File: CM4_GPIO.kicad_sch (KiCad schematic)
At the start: 13 parts, among them J10 Conn_01x03, J4 THD-20-R, J9 Conn_01x03, U12 SI-51005-F, U2 74LVC1G07SE-7

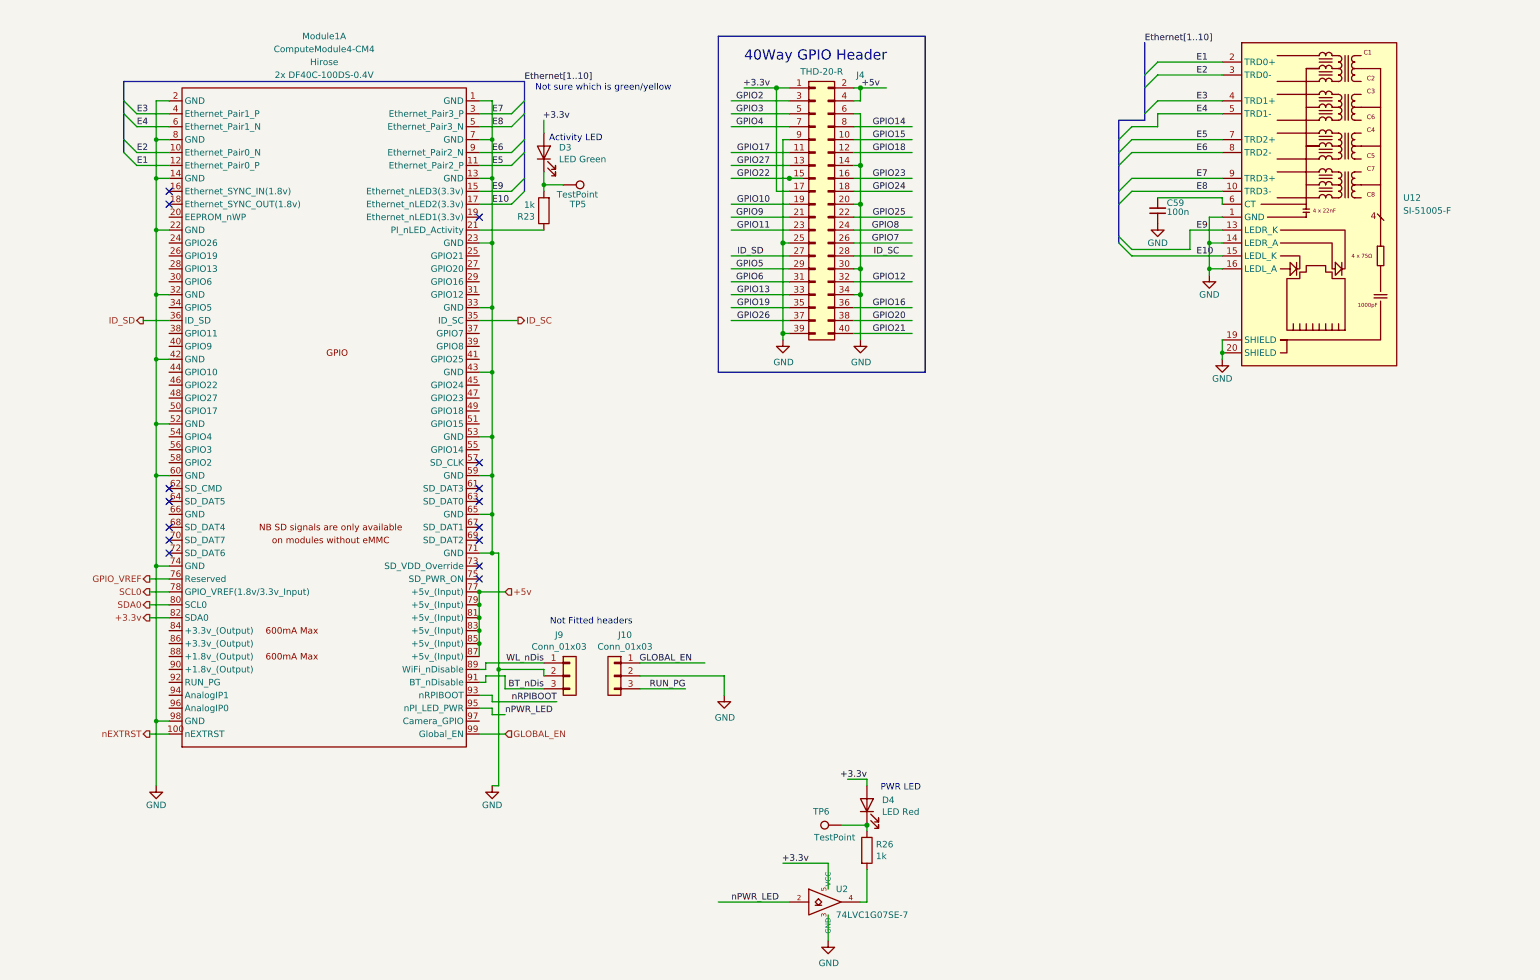
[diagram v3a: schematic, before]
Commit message: Added 3d-models, esd protection, cleaned up and made small start with pcb
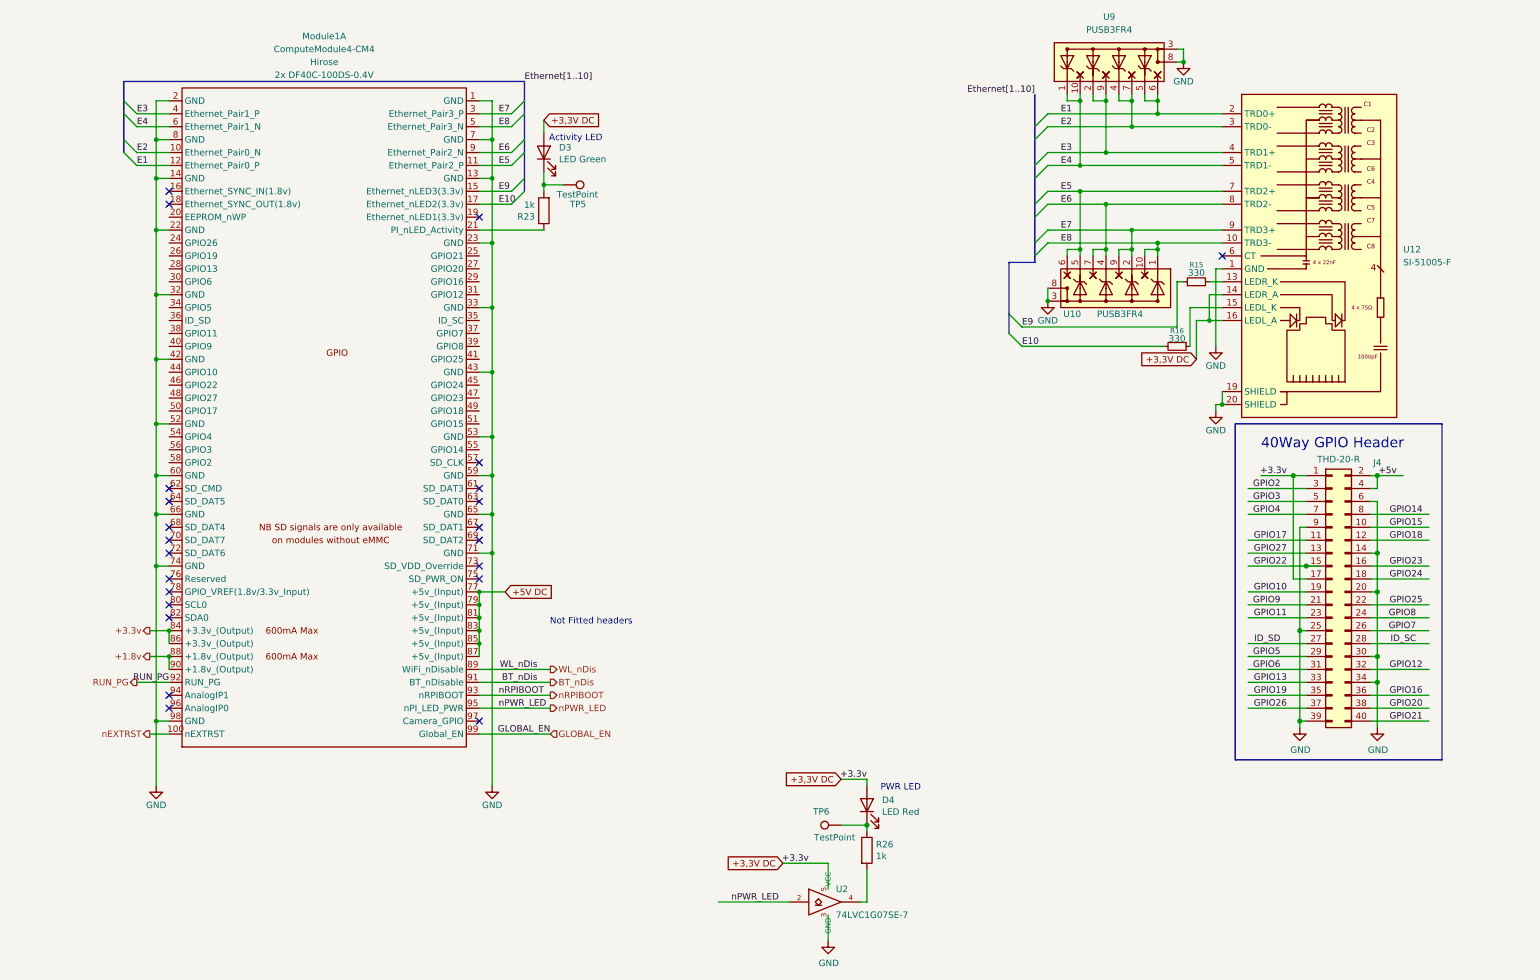
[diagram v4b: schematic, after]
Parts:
- removed C59: 100n, symbol Device:C_Small
- removed J10, J9: Conn_01x03, Connector_PinHeader_2.54mm:PinHeader_1x03_P2.54mm_Vertical, symbol Connector_Generic:Conn_01x03
- added R15, R16: 330, Resistor_SMD:R_0603_1608Metric, symbol Device:R_Small
- added U10, U9: PUSB3FR4, lib:SOT1176-1, symbol PUSB3FR4:PUSB3FR4
- Module1: footprint CM4IO:Raspberry-Pi-4-Compute-Module -> ComputeModule4:Raspberry-Pi-4-Compute-Module
- R23, R26: footprint Resistor_SMD:R_0402_1005Metric -> Resistor_SMD:R_0603_1608Metric
- U12: footprint Ethernet_con:TE_RJ45-8L-B -> SI-51005-F:BEL_SI-51005-F
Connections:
- net +5v: no longer Module1.77 (+5v_(Input)), Module1.79 (+5v_(Input)), Module1.81 (+5v_(Input)), Module1.83 (+5v_(Input)), Module1.85 (+5v_(Input)), Module1.87 (+5v_(Input))
- net E1: now also U9.5 (In_1-), U9.6 (Out_1+)
- net E2: now also U9.4 (In_1+), U9.7 (Out_1+)
- net E3: now also U9.2 (In_1-), U9.9 (Out_1+)
- net E4: now also U9.1 (In_1+), U9.10 (Out_1+)
- net GND: now also Module1.66 (GND), U10.3 (GND), U10.8 (GND), U9.3 (GND), U9.8 (GND); no longer Module1.11 (Ethernet_Pair2_P), Module1.15 (Ethernet_nLED3(3.3v)), Module1.17 (Ethernet_nLED2(3.3v)), Module1.3 (Ethernet_Pair3_P), Module1.5 (Ethernet_Pair3_N), Module1.9 (Ethernet_Pair2_N), U12.10 (TRD3-), U12.13 (LEDR_K), U12.14 (LEDR_A), U12.15 (LEDL_K), U12.16 (LEDL_A), U12.7 (TRD2+), U12.8 (TRD2-), U12.9 (TRD3+)
- net ID_SC: no longer Module1.35 (ID_SC)
- net ID_SD: no longer Module1.36 (ID_SD)
- net RUN_PG: now also Module1.92 (RUN_PG)
- net +3,3V DC: now reaches D3.2 (A)
- net +3,3V DC: now also D4.2 (A), J4.1 (Pin_1), J4.17 (Pin_17), Module1.84 (+3.3v_(Output)), Module1.86 (+3.3v_(Output)), U12.14 (LEDR_A), U12.16 (LEDL_A), U2.5 (VCC)
- net +1.8v: now reaches Module1.88 (+1.8v_(Output))
- net +1.8v: now also Module1.90 (+1.8v_(Output))
- removed net +3.3v: D4.2 (A), J4.1 (Pin_1), J4.17 (Pin_17), Module1.82 (SDA0), U2.5 (VCC)
- net GPIO_VREF: no longer names the net of Module1.76 (Reserved)
- net SCL0: no longer names the net of Module1.78 (GPIO_VREF(1.8v/3.3v_Input))
- net SDA0: no longer names the net of Module1.80 (SCL0)
- new net: R15.2, U12.13 (LEDR_K)
- new net: R16.1, U12.15 (LEDL_K)
- new net +5V DC: Module1.77 (+5v_(Input)), Module1.79 (+5v_(Input)), Module1.81 (+5v_(Input)), Module1.83 (+5v_(Input)), Module1.85 (+5v_(Input)), Module1.87 (+5v_(Input))
- new net E10: Module1.17 (Ethernet_nLED2(3.3v)), R16.2
- new net E5: Module1.11 (Ethernet_Pair2_P), U10.5 (In_1-), U10.6 (Out_1+), U12.7 (TRD2+)
- new net E6: Module1.9 (Ethernet_Pair2_N), U10.4 (In_1+), U10.7 (Out_1+), U12.8 (TRD2-)
- new net E7: Module1.3 (Ethernet_Pair3_P), U10.2 (In_1-), U10.9 (Out_1+), U12.9 (TRD3+)
- new net E8: Module1.5 (Ethernet_Pair3_N), U10.1 (In_1+), U10.10 (Out_1+), U12.10 (TRD3-)
- new net E9: Module1.15 (Ethernet_nLED3(3.3v)), R15.1
- no-connect marks 15 -> 23
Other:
- note removed: "Not sure which is green/yellow"
- moved on the sheet: J4, U12

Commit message: Adjusted the PCB design, changed footprints to 0402 (temp)
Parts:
- R15, R16, R23, R26: footprint Resistor_SMD:R_0603_1608Metric -> Resistor_SMD:R_0402_1005Metric_Pad0.72x0.64mm_HandSolder
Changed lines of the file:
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@@
 			)
 		)
-		(property "Footprint" "Resistor_SMD:R_0603_1608Metric"
+		(property "Footprint" "Resistor_SMD:R_0402_1005Metric_Pad0.72x0.64mm_HandSolder"
 			(at 103.378 48.26 90)
 			(effects
@@
 			)
 		)
-		(property "Footprint" "Resistor_SMD:R_0603_1608Metric"
+		(property "Footprint" "Resistor_SMD:R_0402_1005Metric_Pad0.72x0.64mm_HandSolder"
 			(at 163.322 173.99 90)
 			(effects
@@
 			)
 		)
-		(property "Footprint" "Resistor_SMD:R_0603_1608Metric"
+		(property "Footprint" "Resistor_SMD:R_0402_1005Metric_Pad0.72x0.64mm_HandSolder"
 			(at 226.06 74.93 0)
 			(effects
@@
 			)
 		)
-		(property "Footprint" "Resistor_SMD:R_0603_1608Metric"
+		(property "Footprint" "Resistor_SMD:R_0402_1005Metric_Pad0.72x0.64mm_HandSolder"
 			(at 229.87 62.23 0)
 			(effects

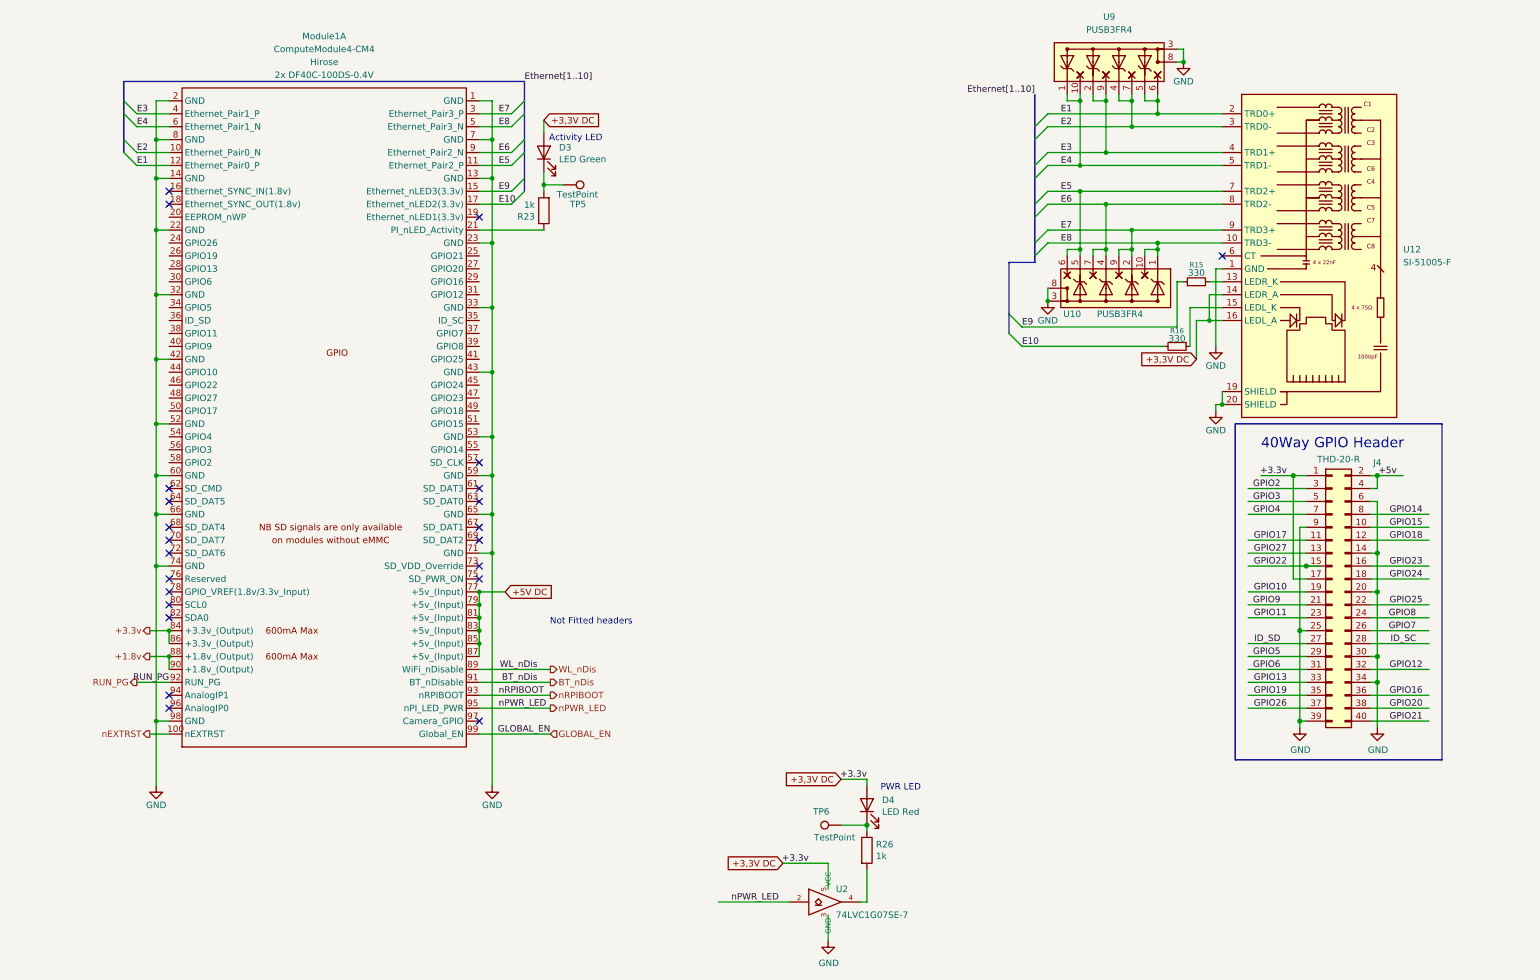
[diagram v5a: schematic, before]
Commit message: heb de GPIO aangepast.
Laten we morgen de stand van zaken bespreken. En overleggen wat we kunnen doen
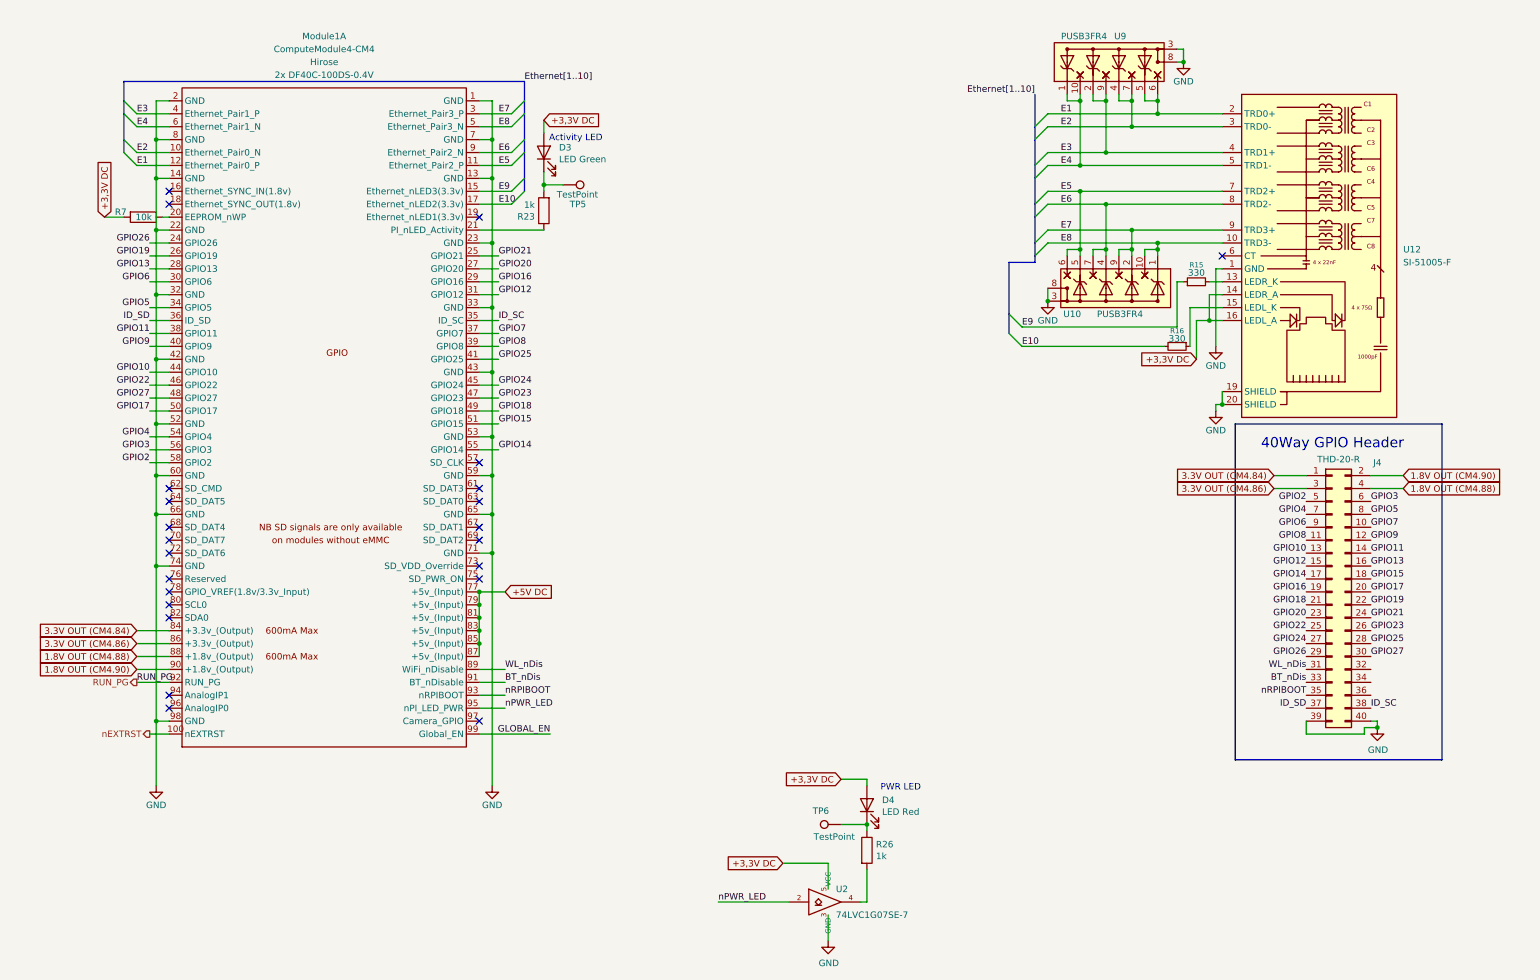
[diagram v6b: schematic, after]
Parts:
- added R7: 10k, Resistor_SMD:R_0402_1005Metric_Pad0.72x0.64mm_HandSolder, symbol Device:R
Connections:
- net +3,3V DC: now also R7.2; no longer J4.1 (Pin_1), J4.17 (Pin_17), Module1.84 (+3.3v_(Output)), Module1.86 (+3.3v_(Output))
- net BT_nDis: now also J4.33 (Pin_33)
- net GND: now also J4.40 (Pin_40); no longer J4.14 (Pin_14), J4.20 (Pin_20), J4.25 (Pin_25), J4.30 (Pin_30), J4.34 (Pin_34), J4.6 (Pin_6), J4.9 (Pin_9)
- net GPIO10: now also J4.13 (Pin_13), Module1.44 (GPIO10); no longer J4.19 (Pin_19)
- net GPIO11: now also J4.14 (Pin_14), Module1.38 (GPIO11); no longer J4.23 (Pin_23)
- net GPIO12: now also J4.15 (Pin_15), Module1.31 (GPIO12); no longer J4.32 (Pin_32)
- net GPIO13: now also J4.16 (Pin_16), Module1.28 (GPIO13); no longer J4.33 (Pin_33)
- net GPIO14: now also J4.17 (Pin_17), Module1.55 (GPIO14); no longer J4.8 (Pin_8)
- net GPIO15: now also J4.18 (Pin_18), Module1.51 (GPIO15); no longer J4.10 (Pin_10)
- net GPIO16: now also J4.19 (Pin_19), Module1.29 (GPIO16); no longer J4.36 (Pin_36)
- net GPIO17: now also J4.20 (Pin_20), Module1.50 (GPIO17); no longer J4.11 (Pin_11)
- net GPIO18: now also J4.21 (Pin_21), Module1.49 (GPIO18); no longer J4.12 (Pin_12)
- net GPIO19: now also J4.22 (Pin_22), Module1.26 (GPIO19); no longer J4.35 (Pin_35)
- net GPIO2: now also J4.5 (Pin_5), Module1.58 (GPIO2); no longer J4.3 (Pin_3)
- net GPIO20: now also J4.23 (Pin_23), Module1.27 (GPIO20); no longer J4.38 (Pin_38)
- net GPIO21: now also J4.24 (Pin_24), Module1.25 (GPIO21); no longer J4.40 (Pin_40)
- net GPIO22: now also J4.25 (Pin_25), Module1.46 (GPIO22); no longer J4.15 (Pin_15)
- net GPIO23: now also J4.26 (Pin_26), Module1.47 (GPIO23); no longer J4.16 (Pin_16)
- net GPIO24: now also J4.27 (Pin_27), Module1.45 (GPIO24); no longer J4.18 (Pin_18)
- net GPIO25: now also J4.28 (Pin_28), Module1.41 (GPIO25); no longer J4.22 (Pin_22)
- net GPIO26: now also J4.29 (Pin_29), Module1.24 (GPIO26); no longer J4.37 (Pin_37)
- net GPIO27: now also J4.30 (Pin_30), Module1.48 (GPIO27); no longer J4.13 (Pin_13)
- net GPIO3: now also J4.6 (Pin_6), Module1.56 (GPIO3); no longer J4.5 (Pin_5)
- net GPIO4: now also Module1.54 (GPIO4)
- net GPIO5: now also J4.8 (Pin_8), Module1.34 (GPIO5); no longer J4.29 (Pin_29)
- net GPIO6: now also J4.9 (Pin_9), Module1.30 (GPIO6); no longer J4.31 (Pin_31)
- net GPIO7: now also J4.10 (Pin_10), Module1.37 (GPIO7); no longer J4.26 (Pin_26)
- net GPIO8: now also J4.11 (Pin_11), Module1.39 (GPIO8); no longer J4.24 (Pin_24)
- net GPIO9: now also J4.12 (Pin_12), Module1.40 (GPIO9); no longer J4.21 (Pin_21)
- net ID_SC: now also J4.38 (Pin_38), Module1.35 (ID_SC); no longer J4.28 (Pin_28)
- net ID_SD: now also J4.37 (Pin_37), Module1.36 (ID_SD); no longer J4.27 (Pin_27)
- net WL_nDis: now also J4.31 (Pin_31)
- net nRPIBOOT: now also J4.35 (Pin_35)
- net at Module1.20 (EEPROM_nWP): now also R7.1
- net +1.8v renamed 1.8V OUT (CM4.88)
- net 1.8V OUT (CM4.88): now also J4.4 (Pin_4); no longer Module1.90 (+1.8v_(Output))
- net +5v renamed 1.8V OUT (CM4.90)
- net 1.8V OUT (CM4.90): now also Module1.90 (+1.8v_(Output)); no longer J4.4 (Pin_4)
- new net 3.3V OUT (CM4.84): J4.1 (Pin_1), Module1.84 (+3.3v_(Output))
- new net 3.3V OUT (CM4.86): J4.3 (Pin_3), Module1.86 (+3.3v_(Output))
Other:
- note removed: "Not Fitted headers"

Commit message: Added lots and lots of traces in PCB design.
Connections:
- net E1 renamed TRD0_P
- net E10 renamed LEDY
- net E2 renamed TRD0_N
- net E3 renamed TRD1_P
- net TRD1_P: now also Module1.6 (Ethernet_Pair1_N); no longer Module1.4 (Ethernet_Pair1_P)
- net E4 renamed TRD1_N
- net TRD1_N: now also Module1.4 (Ethernet_Pair1_P); no longer Module1.6 (Ethernet_Pair1_N)
- net E5 renamed TRD2_P
- net E6 renamed TRD2_N
- net E7 renamed TRD3_P
- net E8 renamed TRD3_N
- net E9 renamed LEDG
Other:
- moved on the sheet: D3, R16, R23, TP5
